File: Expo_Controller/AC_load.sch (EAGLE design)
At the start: 10 parts

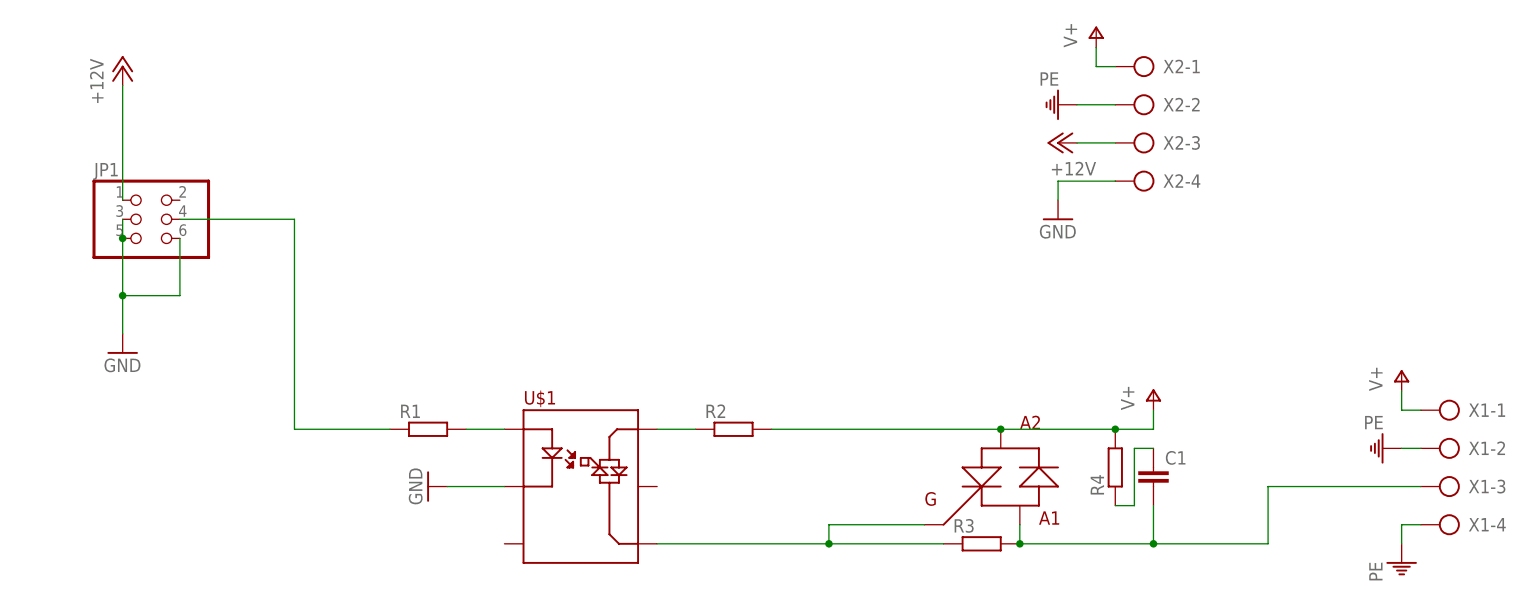
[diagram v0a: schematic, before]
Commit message: Закончил разводку высоковольтного модуля
Signed-off-by: remixvit <remixvi@gmail.comt>
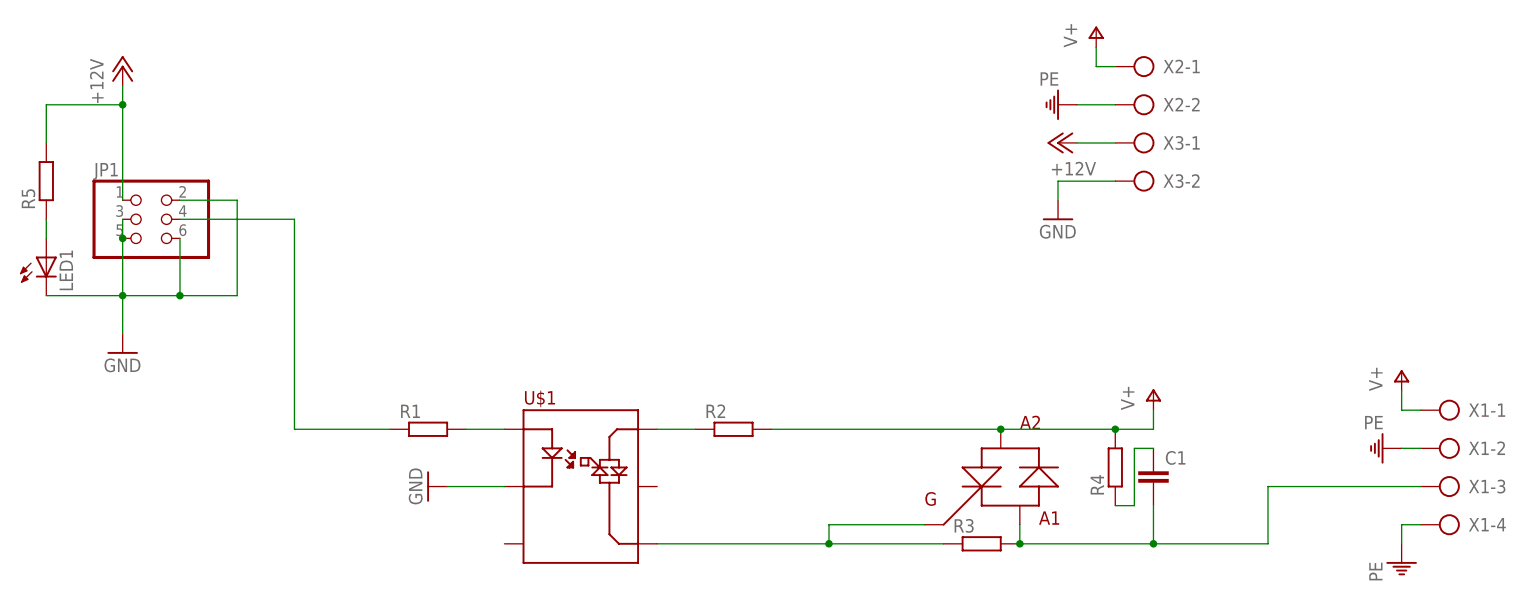
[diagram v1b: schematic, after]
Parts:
- removed TRIAC1: BTB16_FLAT, Semistors:BTB16_FLAT
- added LED1: (no value), led:LEDSML1206
- added R5: (no value), rcl:R-EU_M1206
- added U$2: BTB16, Semistors:BTB16
- added X3: (no value), con-ptr500:AK500/2
- X2: device con-ptr500:AK500/4 -> con-ptr500:AK500/2
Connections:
- new net N$14: LED1.A, R5.1
- net +12V: now also R5.2, X3-1.KL; no longer X2-3.KL
- net GND: now also JP1.2, LED1.C, X3-2.KL; no longer X2-4.KL
- net N$2: now also U$2.A1; no longer TRIAC1.A1
- net N$4: now also U$2.G; no longer TRIAC1.G
- net V+: now also U$2.A2; no longer TRIAC1.A2
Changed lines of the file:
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@@
 <?xml version="1.0" encoding="utf-8"?>
 <!DOCTYPE eagle SYSTEM "eagle.dtd">
-<eagle version="6.5.0">
+<eagle version="7.1.0">
 <drawing>
 <settings>
@@
 <parts>
 <part name="U$1" library="OpticalSwitch" deviceset="MOC3043" device=""/>
-<part name="TRIAC1" library="Semistors" deviceset="BTB16_FLAT" device=""/>
 <part name="X1" library="con-ptr500" deviceset="AK500/4" device=""/>
 <part name="PE1" library="supply1" deviceset="PE" device=""/>
@@
 <part name="P+3" library="supply1" deviceset="V+" device=""/>
 <part name="PE2" library="supply1" deviceset="PE" device=""/>
-<part name="X2" library="con-ptr500" deviceset="AK500/4" device=""/>
 <part name="P+4" library="supply1" deviceset="V+" device=""/>
 <part name="PE3" library="supply1" deviceset="PE" device=""/>
 <part name="GND3" library="supply1" deviceset="GND" device=""/>
 <part name="P+5" library="supply1" deviceset="+12V" device=""/>
+<part name="X2" library="con-ptr500" deviceset="AK500/2" device=""/>
+<part name="X3" library="con-ptr500" deviceset="AK500/2" device=""/>
+<part name="U$2" library="Semistors" deviceset="BTB16" device=""/>
+<part name="LED1" library="led" deviceset="LED" device="SML1206"/>
+<part name="R5" library="rcl" deviceset="R-EU_" device="M1206"/>
 </parts>
 <sheets>
@@
 <instances>
 <instance part="U$1" gate="G$1" x="0" y="0"/>
-<instance part="TRIAC1" gate="G$1" x="58.42" y="0"/>
 <instance part="X1" gate="-1" x="116.84" y="10.16" rot="MR0"/>
 <instance part="X1" gate="-2" x="116.84" y="5.08" rot="MR0"/>
@@
 <instance part="P+3" gate="1" x="76.2" y="12.7"/>
 <instance part="PE2" gate="M" x="106.68" y="5.08" rot="R270"/>
-<instance part="X2" gate="-1" x="76.2" y="55.88" rot="MR0"/>
-<instance part="X2" gate="-2" x="76.2" y="50.8" rot="MR0"/>
-<instance part="X2" gate="-3" x="76.2" y="45.72" rot="MR0"/>
-<instance part="X2" gate="-4" x="76.2" y="40.64" rot="MR0"/>
 <instance part="P+4" gate="1" x="68.58" y="60.96"/>
 <instance part="PE3" gate="M" x="63.5" y="50.8" rot="R270"/>
 <instance part="GND3" gate="1" x="63.5" y="35.56"/>
 <instance part="P+5" gate="1" x="63.5" y="45.72" rot="R90"/>
+<instance part="X2" gate="-1" x="76.2" y="55.88" rot="MR0"/>
+<instance part="X2" gate="-2" x="76.2" y="50.8" rot="MR0"/>
+<instance part="X3" gate="-1" x="76.2" y="45.72" rot="MR0"/>
+<instance part="X3" gate="-2" x="76.2" y="40.64" rot="MR0"/>
+<instance part="U$2" gate="G$1" x="58.42" y="0"/>
+<instance part="LED1" gate="G$1" x="-71.12" y="30.48"/>
+<instance part="R5" gate="G$1" x="-71.12" y="40.64" rot="R90"/>
 </instances>
 <busses>
@@
 </segment>
 <segment>
-<pinref part="TRIAC1" gate="G$1" pin="A2"/>
 <pinref part="R2" gate="G$1" pin="2"/>
+<wire x1="71.12" y1="7.62" x2="55.88" y2="7.62" width="0.1524" layer="91"/>
+<pinref part="R4" gate="G$1" pin="2"/>
+<pinref part="P+3" gate="1" pin="V+"/>
 <wire x1="55.88" y1="7.62" x2="25.4" y2="7.62" width="0.1524" layer="91"/>
-<pinref part="R4" gate="G$1" pin="2"/>
-<wire x1="71.12" y1="7.62" x2="55.88" y2="7.62" width="0.1524" layer="91"/>
-<junction x="55.88" y="7.62"/>
-<pinref part="P+3" gate="1" pin="V+"/>
 <wire x1="71.12" y1="7.62" x2="76.2" y2="7.62" width="0.1524" layer="91"/>
 <wire x1="76.2" y1="7.62" x2="76.2" y2="10.16" width="0.1524" layer="91"/>
 <junction x="71.12" y="7.62"/>
-</segment>
-<segment>
-<pinref part="X2" gate="-1" pin="KL"/>
+<pinref part="U$2" gate="G$1" pin="A2"/>
+<junction x="55.88" y="7.62"/>
+</segment>
+<segment>
 <pinref part="P+4" gate="1" pin="V+"/>
 <wire x1="71.12" y1="55.88" x2="68.58" y2="55.88" width="0.1524" layer="91"/>
 <wire x1="68.58" y1="55.88" x2="68.58" y2="58.42" width="0.1524" layer="91"/>
+<pinref part="X2" gate="-1" pin="KL"/>
 </segment>
 </net>
@@
 </segment>
 <segment>
-<pinref part="X2" gate="-2" pin="KL"/>
 <pinref part="PE3" gate="M" pin="PE"/>
 <wire x1="71.12" y1="50.8" x2="66.04" y2="50.8" width="0.1524" layer="91"/>
+<pinref part="X2" gate="-2" pin="KL"/>
 </segment>
 </net>
@@
 <wire x1="-53.34" y1="25.4" x2="-53.34" y2="33.02" width="0.1524" layer="91"/>
 <junction x="-60.96" y="25.4"/>
-</segment>
-<segment>
-<pinref part="X2" gate="-4" pin="KL"/>
+<wire x1="-53.34" y1="25.4" x2="-45.72" y2="25.4" width="0.1524" layer="91"/>
+<wire x1="-45.72" y1="25.4" x2="-45.72" y2="38.1" width="0.1524" layer="91"/>
+<junction x="-53.34" y="25.4"/>
+<pinref part="JP1" gate="A" pin="2"/>
+<wire x1="-45.72" y1="38.1" x2="-53.34" y2="38.1" width="0.1524" layer="91"/>
+<pinref part="LED1" gate="G$1" pin="C"/>
+<wire x1="-71.12" y1="25.4" x2="-60.96" y2="25.4" width="0.1524" layer="91"/>
+</segment>
+<segment>
 <pinref part="GND3" gate="1" pin="GND"/>
 <wire x1="71.12" y1="40.64" x2="63.5" y2="40.64" width="0.1524" layer="91"/>
 <wire x1="63.5" y1="40.64" x2="63.5" y2="38.1" width="0.1524" layer="91"/>
+<pinref part="X3" gate="-2" pin="KL"/>
 </segment>
 </net>
@@
 <pinref part="JP1" gate="A" pin="1"/>
 <pinref part="P+2" gate="1" pin="+12V"/>
-<wire x1="-60.96" y1="38.1" x2="-60.96" y2="53.34" width="0.1524" layer="91"/>
-</segment>
-<segment>
-<pinref part="X2" gate="-3" pin="KL"/>
+<wire x1="-60.96" y1="38.1" x2="-60.96" y2="50.8" width="0.1524" layer="91"/>
+<pinref part="R5" gate="G$1" pin="2"/>
+<wire x1="-60.96" y1="50.8" x2="-60.96" y2="53.34" width="0.1524" layer="91"/>
+<wire x1="-71.12" y1="45.72" x2="-71.12" y2="50.8" width="0.1524" layer="91"/>
+<wire x1="-71.12" y1="50.8" x2="-60.96" y2="50.8" width="0.1524" layer="91"/>
+<junction x="-60.96" y="50.8"/>
+</segment>
+<segment>
 <pinref part="P+5" gate="1" pin="+12V"/>
 <wire x1="71.12" y1="45.72" x2="66.04" y2="45.72" width="0.1524" layer="91"/>
+<pinref part="X3" gate="-1" pin="KL"/>
 </segment>
 </net>
 <net name="N$2" class="0">
 <segment>
-<pinref part="TRIAC1" gate="G$1" pin="A1"/>
 <pinref part="R3" gate="G$1" pin="2"/>
 <wire x1="58.42" y1="-5.08" x2="58.42" y2="-7.62" width="0.1524" layer="91"/>
@@
 <wire x1="111.76" y1="0" x2="91.44" y2="0" width="0.1524" layer="91"/>
 <wire x1="91.44" y1="0" x2="91.44" y2="-7.62" width="0.1524" layer="91"/>
+<pinref part="U$2" gate="G$1" pin="A1"/>
 </segment>
 </net>
@@
 <wire x1="10.16" y1="-7.62" x2="33.02" y2="-7.62" width="0.1524" layer="91"/>
 <wire x1="33.02" y1="-7.62" x2="33.02" y2="-5.08" width="0.1524" layer="91"/>
-<pinref part="TRIAC1" gate="G$1" pin="G"/>
 <wire x1="33.02" y1="-5.08" x2="45.72" y2="-5.08" width="0.1524" layer="91"/>
 <pinref part="R3" gate="G$1" pin="1"/>
 <wire x1="48.26" y1="-7.62" x2="33.02" y2="-7.62" width="0.1524" layer="91"/>
 <junction x="33.02" y="-7.62"/>
+<pinref part="U$2" gate="G$1" pin="G"/>
 </segment>
 </net>
@@
 </segment>
 </net>
+<net name="N$14" class="0">
+<segment>
+<pinref part="R5" gate="G$1" pin="1"/>
+<pinref part="LED1" gate="G$1" pin="A"/>
+<wire x1="-71.12" y1="35.56" x2="-71.12" y2="33.02" width="0.1524" layer="91"/>
+</segment>
+</net>
